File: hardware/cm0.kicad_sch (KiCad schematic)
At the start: 0 parts

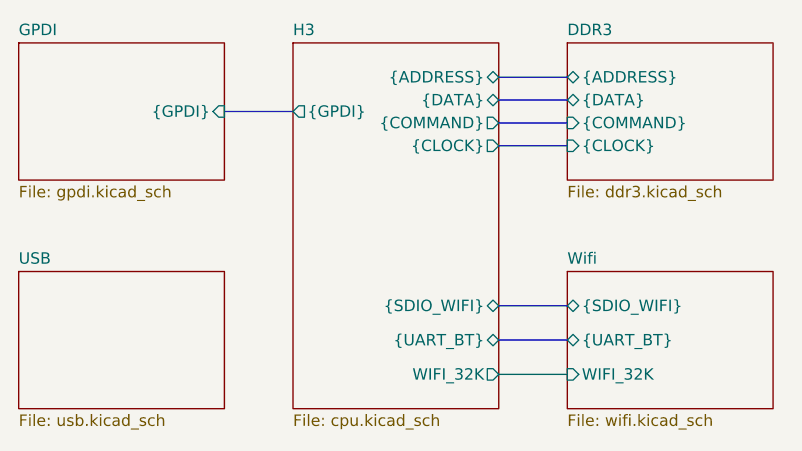
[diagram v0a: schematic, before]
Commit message: Decoupled DDR3 and drew RJ45 connector
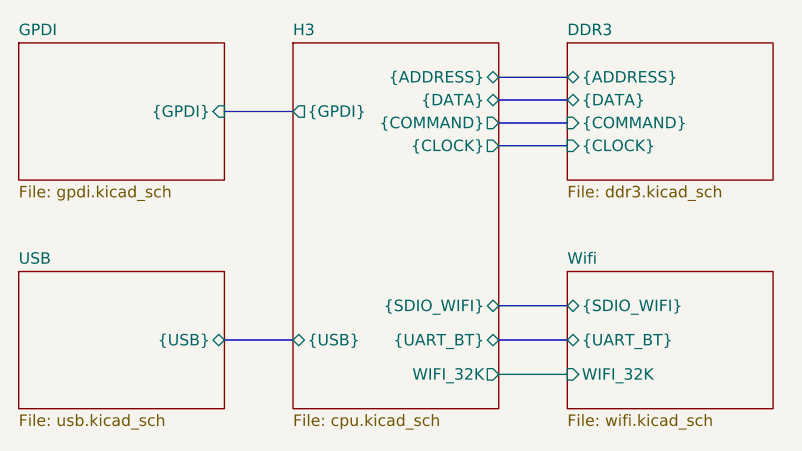
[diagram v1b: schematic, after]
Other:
- sheet H3 ports: added {USB}; removed none
- sheet USB ports: added {USB}; removed none
- company: (none) -> Icy Electronics
- title: (none) -> Icepi CM0
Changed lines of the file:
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@@
 	(generator_version "9.0")
 	(paper "A4")
+	(title_block
+		(title "Icepi CM0")
+		(date "2025-11-03")
+		(rev "v1.0")
+		(company "Icy Electronics")
+		(comment 1 "Chengyin Yao (cheyao)")
+		(comment 2 "https://github.com/cheyao/icepi-cm0")
+	)
 	(bus
 		(pts
@@
 		(pts
 			(xy 124.46 62.23) (xy 132.08 62.23)
+		)
+		(stroke
+			(width 0)
+			(type default)
+		)
+	)
+	(bus
+		(pts
+			(xy 93.98 66.04) (xy 101.6 66.04)
 		)
 		(stroke
@@
 			)
 		)
+		(pin "{USB}" bidirectional
+			(at 93.98 66.04 0)
+			(effects
+				(font
+					(size 1.27 1.27)
+				)
+				(justify right)
+			)
+		)
 		(instances
 			(project "cm0"
@@
 			(effects
 				(font
+					(size 1.27 1.27)
+				)
+				(justify left)
+			)
+		)
+		(pin "{USB}" bidirectional
+			(at 101.6 66.04 180)
+			(effects
+				(font
